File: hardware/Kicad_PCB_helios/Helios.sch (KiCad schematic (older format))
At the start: 19 parts, among them P1 USB_B, P2 CONN_01X25-SHIELD, U1 IP4220CZ6

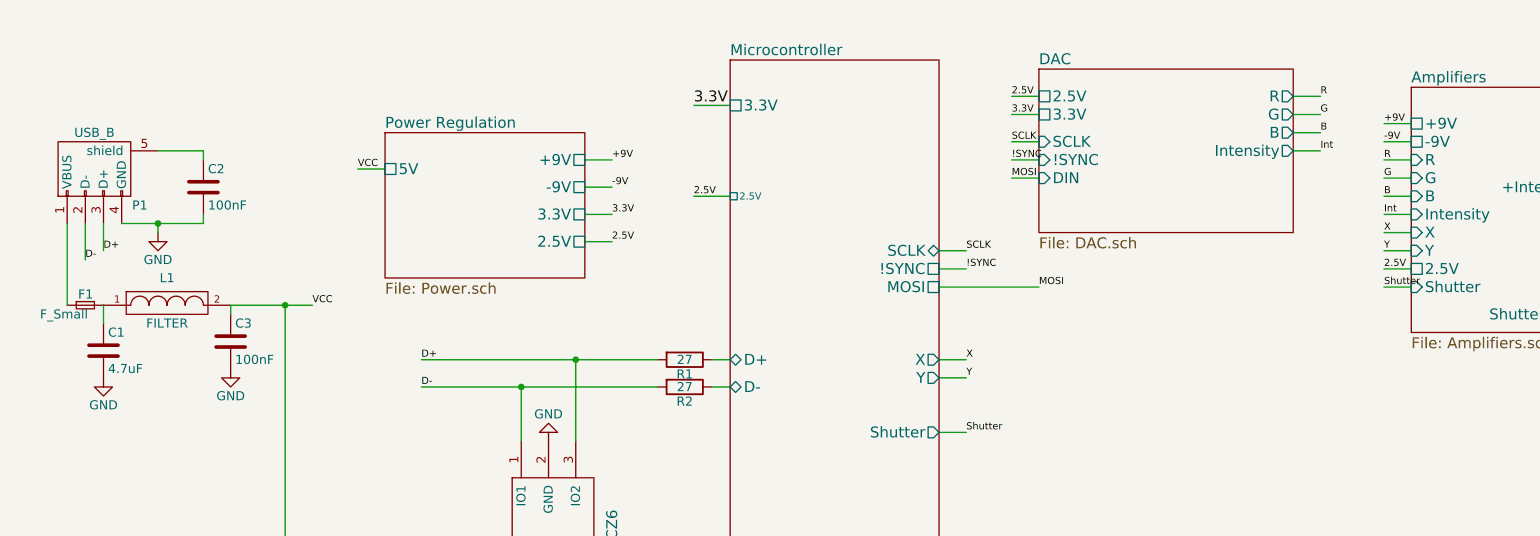
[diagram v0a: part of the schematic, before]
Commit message: Dodano 2 zewnętrzne 16 bitowe układy DAC
Podłączono VREF do wewnętrznych DAC

Wszystko działa na jednej magistrali SPI
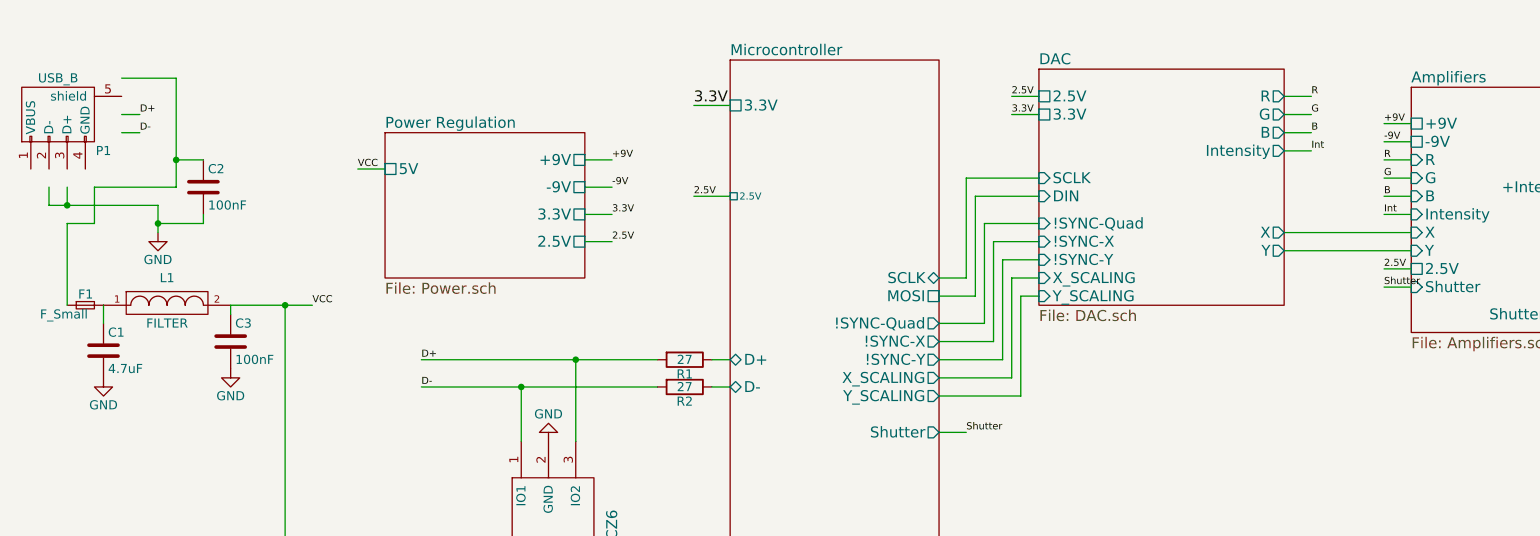
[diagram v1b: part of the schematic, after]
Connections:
- net labels removed: !SYNC, MOSI, SCLK, X, Y
- wire segments 102 -> 122
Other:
- moved on the sheet: P1

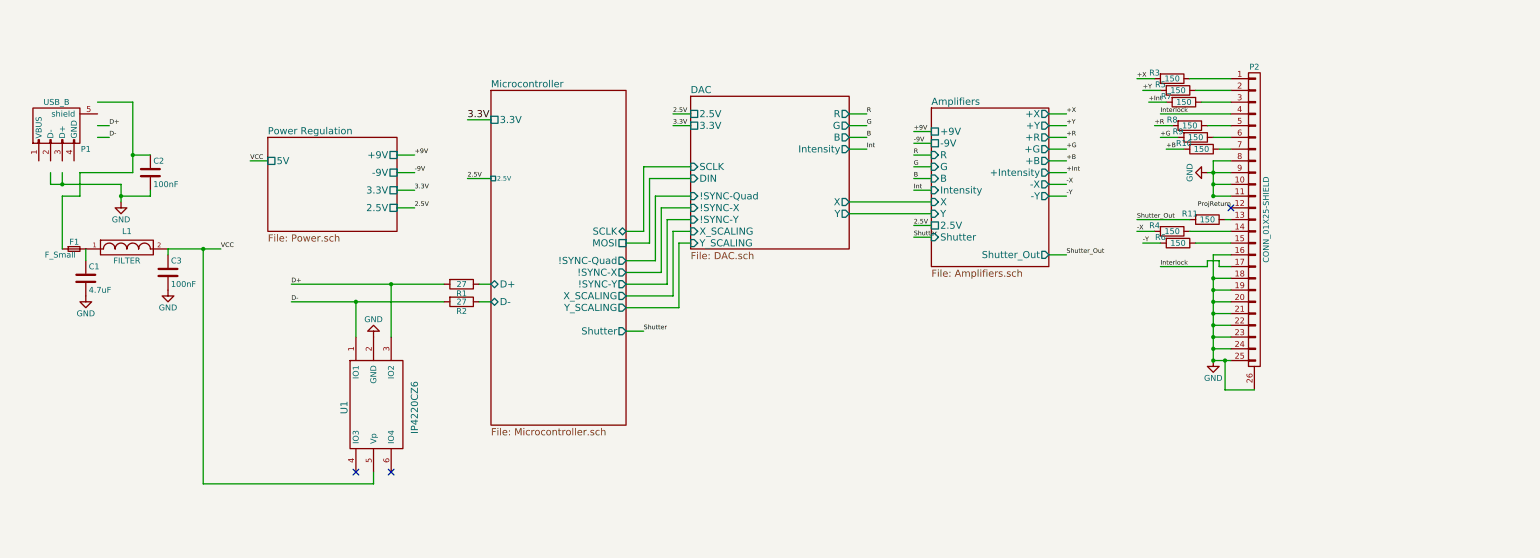
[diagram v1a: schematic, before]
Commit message: Updated PCB Layout
Changed connector to IDC
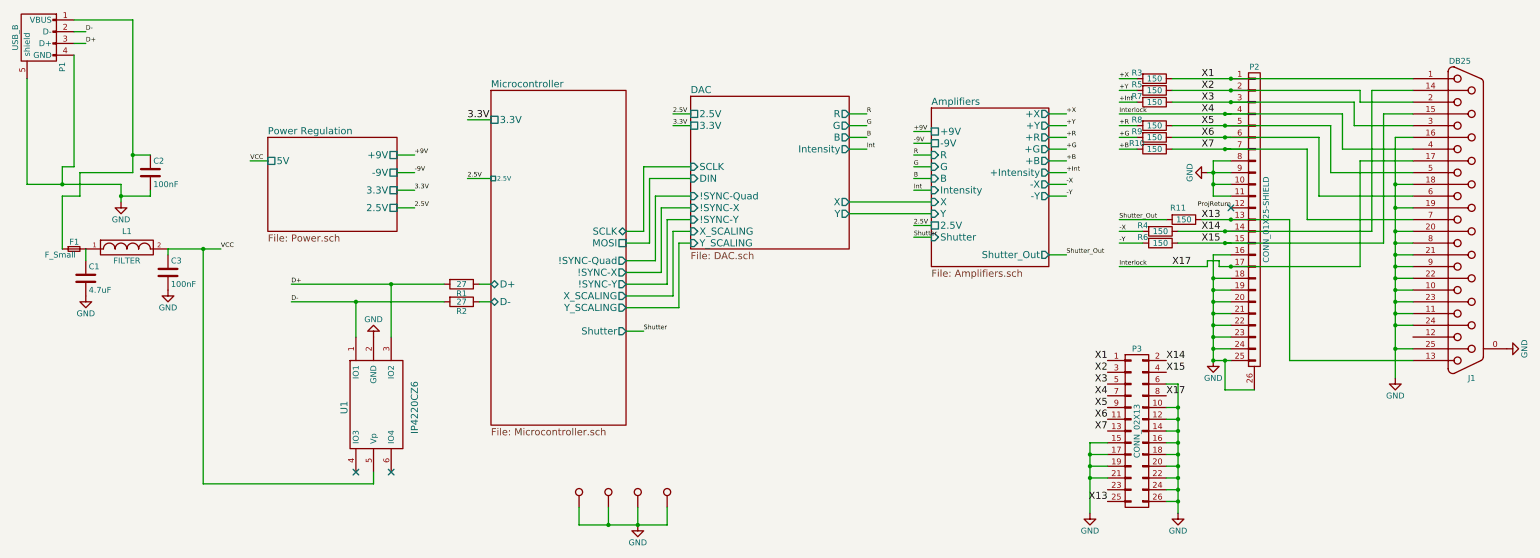
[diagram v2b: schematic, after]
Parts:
- added J1: DB25, Connectors:DB25FD, symbol DB25
- added P3: CONN_02X13, Connectors:IDC_Header_Straight_26pins, symbol CONN_02X13
- added W1, W2, W3, W4: TEST_1P, Connectors:1pin, symbol TEST_1P
- C2, C3: footprint Capacitors_SMD:C_0402 -> Capacitors_SMD:C_0603
- P1: footprint Connect:USB_B -> (none)
- P2: footprint personal:DB25 -> (none)
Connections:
- net labels added: X1, X13, X14, X15, X17, X2, X3, X4, X5, X6, X7
- wire segments 122 -> 185
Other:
- moved on the sheet: R10, R11, R3, R4, R5, R6, R7, R8, R9
